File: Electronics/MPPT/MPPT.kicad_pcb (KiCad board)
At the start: 2 copper layers, 125 parts, among them J1 Solar Array, J2 Battery, J3 Car Power, J4 CAN_In, J5 CAN_Out, Q1 200N25N, Q2 200N25N, SW1 RESET, SW2 CAN Address, U1 PQMC3-D12-S9-S, U2 Nucleo_L432KC, U3 UCC37321, U4 INA213, U5 ADM3055E, U6 INA213, U7 CDSOT23-T24CAN

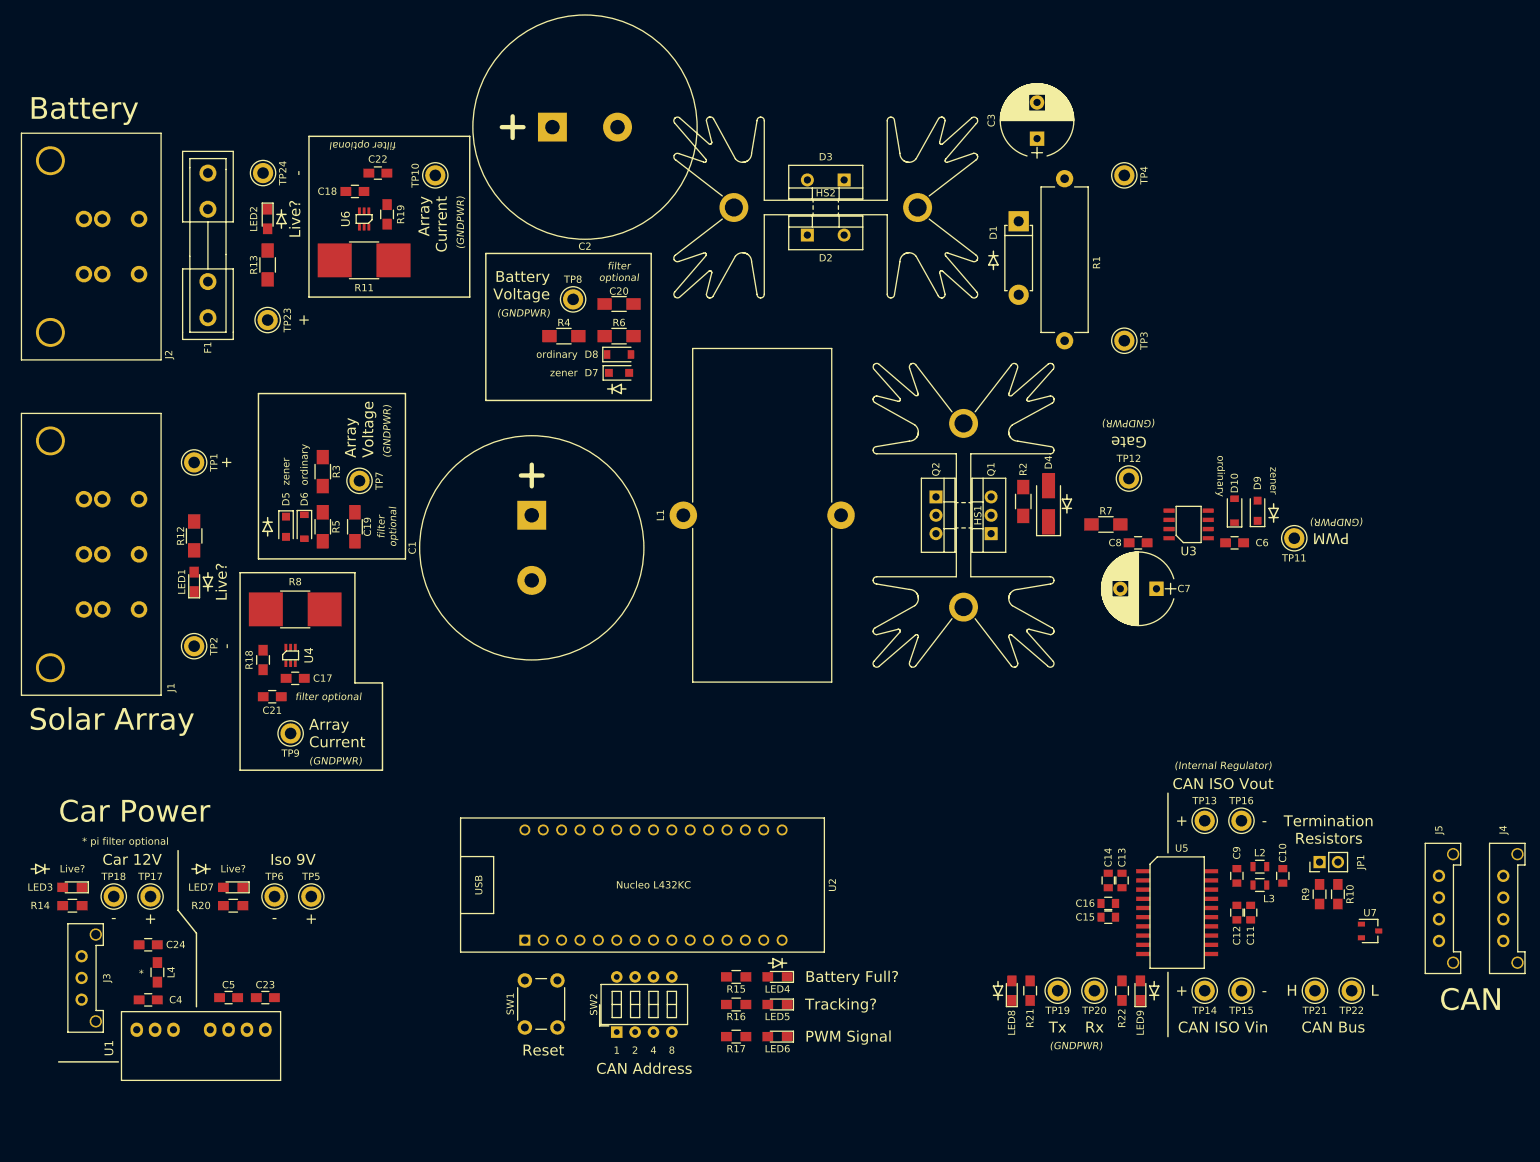
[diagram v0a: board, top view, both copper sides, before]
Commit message: MPPT: Laid out and wired much of the board. Could use much work still.
Still need to wire up CAN block and sensors; kicad is being funny about clearances around the INA chips. Also need to move filters closer to the Nucleo rather than centered around the sensors. Whole board could be compacted further.
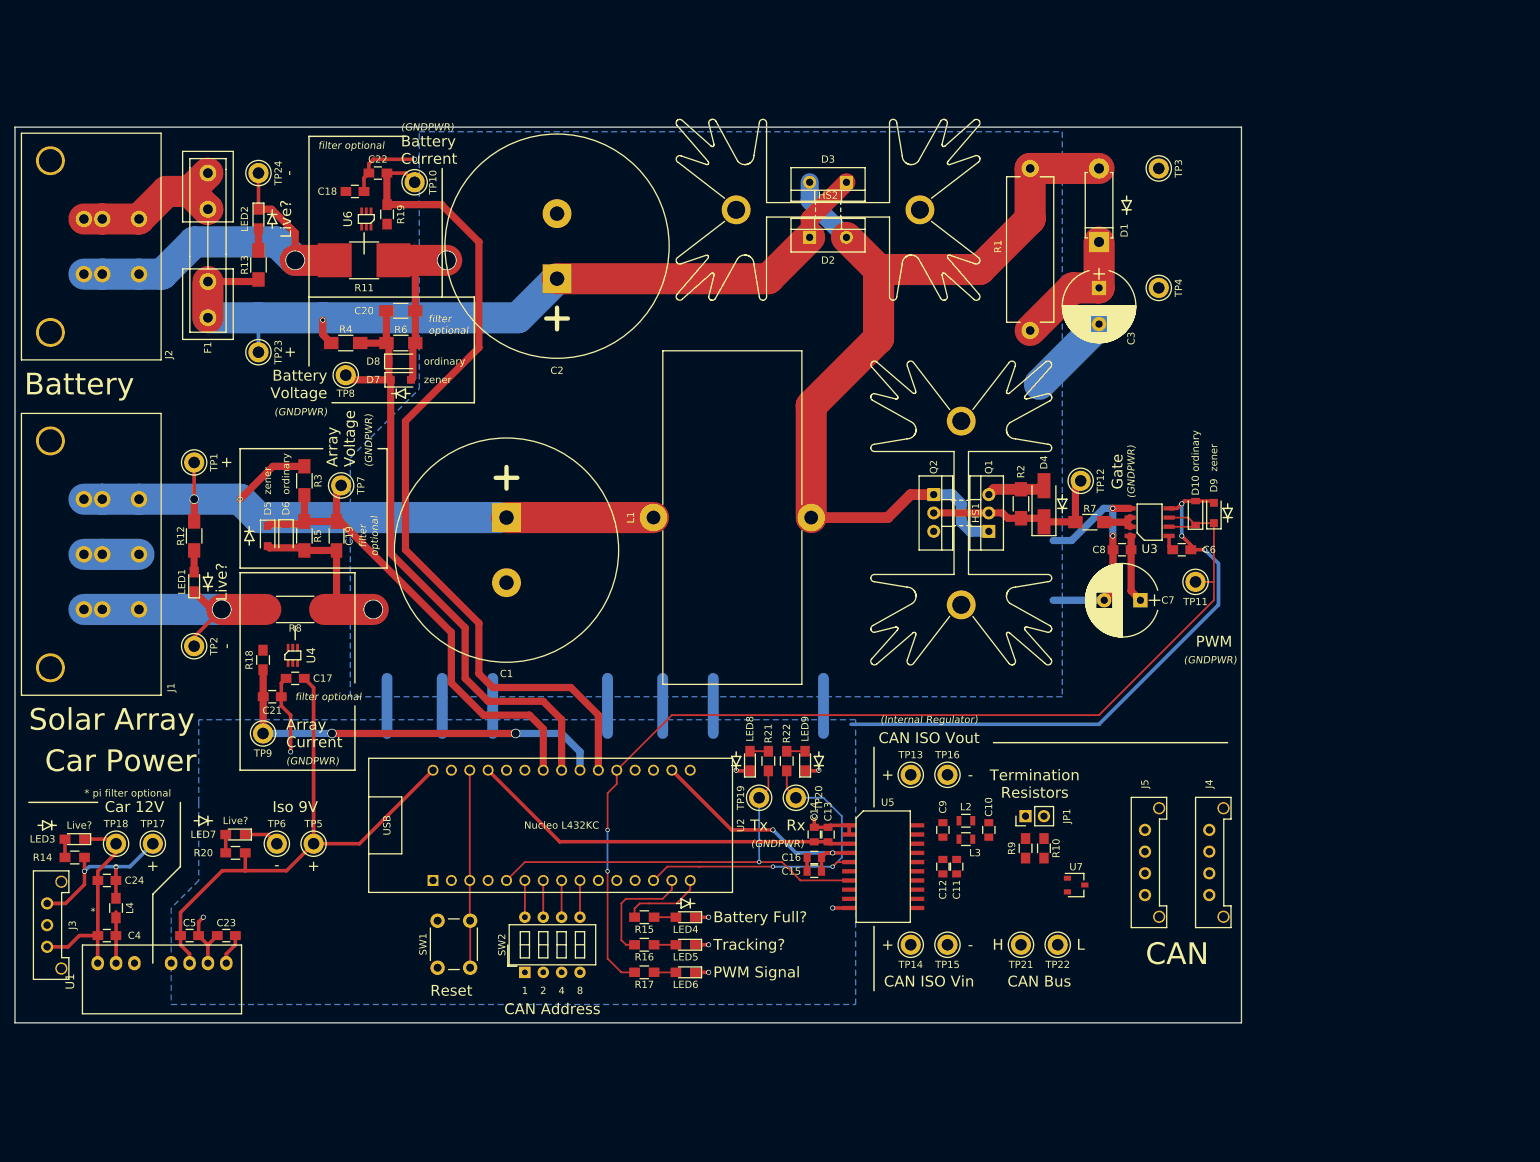
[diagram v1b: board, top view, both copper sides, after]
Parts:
- R8: footprint Resistors_SMD:R_2816_HandSoldering -> Resistors_SMD:R_2512_HandSoldering
- moved R22 56.2 mm to (137.8, 118.7)
- moved LED9 56.2 mm to (140.3, 118.7)
- moved REF** 56.2 mm to (142.2, 118.7)
- moved TP20 49.1 mm to (139.1, 123.8)
- moved TP19 49.1 mm to (134.0, 123.8)
- moved LED8 48.1 mm to (132.7, 118.7)
- moved R21 48.1 mm to (135.3, 118.7)
- moved REF** 48.1 mm to (130.8, 118.7)
- moved C11 41.1 mm to (161.3, 133.3)
- moved C12 41.1 mm to (159.4, 133.3)
- moved C13 41.1 mm to (143.5, 128.9)
- moved C14 41.1 mm to (141.6, 128.9)
- moved C15 41.1 mm to (141.6, 134.0)
- moved C16 41.1 mm to (141.6, 132.1)
- moved C9 41.1 mm to (159.4, 128.3)
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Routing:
- net GNDPWR: track 0.00 -> 240.6 mm, vias 0 -> 17
- net /PWM: track 0.00 -> 147.0 mm, vias 0 -> 2
- net Net-(D1-Pad2): track 0.00 -> 124.0 mm
- net /+Batt: track 0.00 -> 118.7 mm, vias 0 -> 1
- net /Battery_Current: track 0.00 -> 118.2 mm
- net /+Arr: track 0.00 -> 98.1 mm, vias 0 -> 2
- net /Battery_Voltage: track 0.00 -> 88.1 mm
- net +9VA: track 0.00 -> 88.0 mm
- net /Array_Voltage: track 0.00 -> 68.9 mm
- net /CAN_Tx: track 0.00 -> 62.6 mm, vias 0 -> 1
- net /Array_Current: track 0.00 -> 56.2 mm, vias 0 -> 2
- net +5V: track 0.00 -> 54.1 mm
- net (no net): track 0.00 -> 53.4 mm
- net /-Batt: track 0.00 -> 52.8 mm, vias 0 -> 1
- net /CAN_Rx: track 0.00 -> 47.3 mm, vias 0 -> 2
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- added copper zone on B.Cu, net GNDPWR
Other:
- board outline added: 169.5 x 123.8 mm
- net class HighPower added: clearance 0.5, trace_width 4.3, via_dia 2.7, via_drill 2.5
- net class HighPowerHalf added: clearance 0.3, trace_width 2.5, via_dia 2.7, via_drill 2.5
- net class HighPowerSignal added: clearance 0.2, trace_width 1, via_dia 1.3, via_drill 1.1
- net class HighPowerSmall added: clearance 0.2, trace_width 1.5, via_dia 1.8, via_drill 1.6
- net class LowPower added: clearance 0.2, trace_width 0.5, via_dia 0.7, via_drill 0.5
- net class Signal added: clearance 0.2, trace_width 0.25, via_dia 0.6, via_drill 0.4
- board text added: "Battery Current"

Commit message: MPPT: Import changes from schematic; move sensor filters to Nucleo; compact power electronics further.
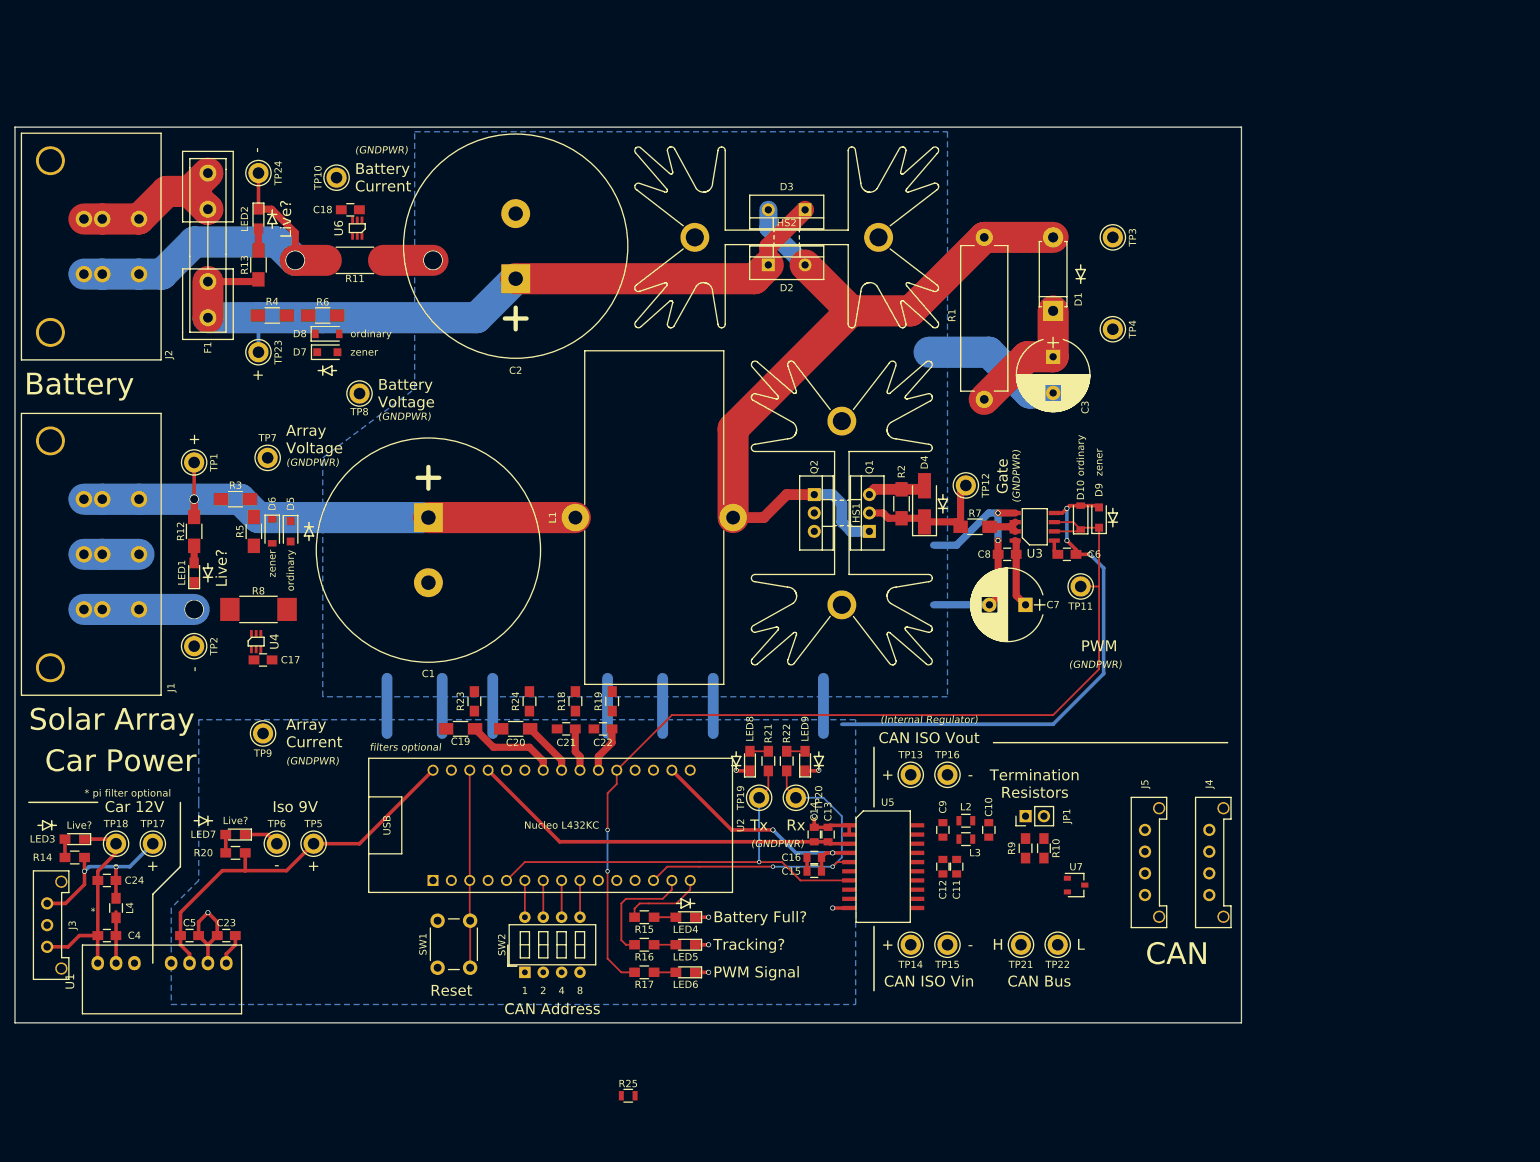
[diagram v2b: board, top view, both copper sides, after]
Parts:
- added R23: 1.7k, Resistors_SMD:R_0805_HandSoldering, F.Cu at (94.6, 110.5)
- added R24: 1.7k, Resistors_SMD:R_0805_HandSoldering, F.Cu at (102.2, 110.5)
- added R25: 0, Resistors_SMD:R_0805, F.Cu at (115.9, 165.0)
- C19, C20, C21, C22: value ?C -> 1uF
- R11: value 10m -> 2m; footprint Resistors_SMD:R_2816_HandSoldering -> Resistors_SMD:R_2512_HandSoldering
- R18, R19: value ?R -> 1.7k
- R8: value 10m -> 2m
- U4, U6: value INA213 -> INA210
- moved C22 82.9 mm to (112.4, 114.3)
- moved R19 74.2 mm to (113.7, 110.5), turned to 270 degrees
- moved C20 59.9 mm to (100.3, 114.3), turned to 180 degrees
- moved R18 43.6 mm to (108.6, 110.5)
- moved C21 40.9 mm to (107.3, 114.3), turned to 180 degrees
- moved C19 31.7 mm to (92.7, 114.3), turned to 180 degrees
- moved HS1 16.5 mm to (145.4, 84.5)
- moved Q1 16.5 mm to (149.2, 87.0)
- moved Q2 16.5 mm to (141.6, 81.9)
- moved R2 16.5 mm to (153.7, 83.2)
- moved REF** 16.5 mm to (159.4, 83.2)
- moved D4 16.5 mm to (156.8, 83.2)
- moved C6 15.9 mm to (176.5, 90.2)
- moved C7 15.9 mm to (170.8, 97.2)
- moved C8 15.9 mm to (168.3, 90.2)
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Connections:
- D5 pad 1: /Array_Voltage -> Net-(D5-Pad1)
- D6 pad 1: /Array_Voltage -> Net-(D5-Pad1)
- D7 pad 1: /Battery_Voltage -> Net-(D7-Pad1)
- D8 pad 1: /Battery_Voltage -> Net-(D7-Pad1)
- R3 pad 2: /Array_Voltage -> Net-(D5-Pad1)
- R4 pad 2: /Battery_Voltage -> Net-(D7-Pad1)
- R5 pad 1: /Array_Voltage -> Net-(D5-Pad1)
- R6 pad 1: /Battery_Voltage -> Net-(D7-Pad1)
- U5 pad 12: Net-(C10-Pad2) -> Net-(R25-Pad1)
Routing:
- net /Battery_Current: track 118.2 -> 6.50 mm
- net /Battery_Voltage: track 88.1 -> 7.52 mm
- net GNDPWR: track 240.6 -> 179.5 mm, vias 17 -> 14
- net /Array_Voltage: track 68.9 -> 12.5 mm
- net /Array_Current: track 56.2 -> 6.01 mm, vias 2 -> 0
- net +9VA: track 88.0 -> 64.6 mm
- net /+Arr: track 98.1 -> 75.9 mm, vias 2 -> 1
- net /-Arr: track 36.6 -> 16.5 mm
- net Net-(D1-Pad2): track 124.0 -> 109.9 mm
- net /+Batt: track 118.7 -> 107.7 mm, vias 1 -> 0
- net /PWM: track 147.0 -> 136.1 mm
- net /Drive_PWM: track 26.1 -> 19.5 mm
- net /-Batt: track 52.8 -> 51.6 mm
- net Net-(LED1-Pad2): track 3.00 -> 2.36 mm
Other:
- board text added: "filters optional"
- board text removed: "filter optional"

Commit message: MPPT: Shift Nucleo into more compact location; move sensor test points into position.
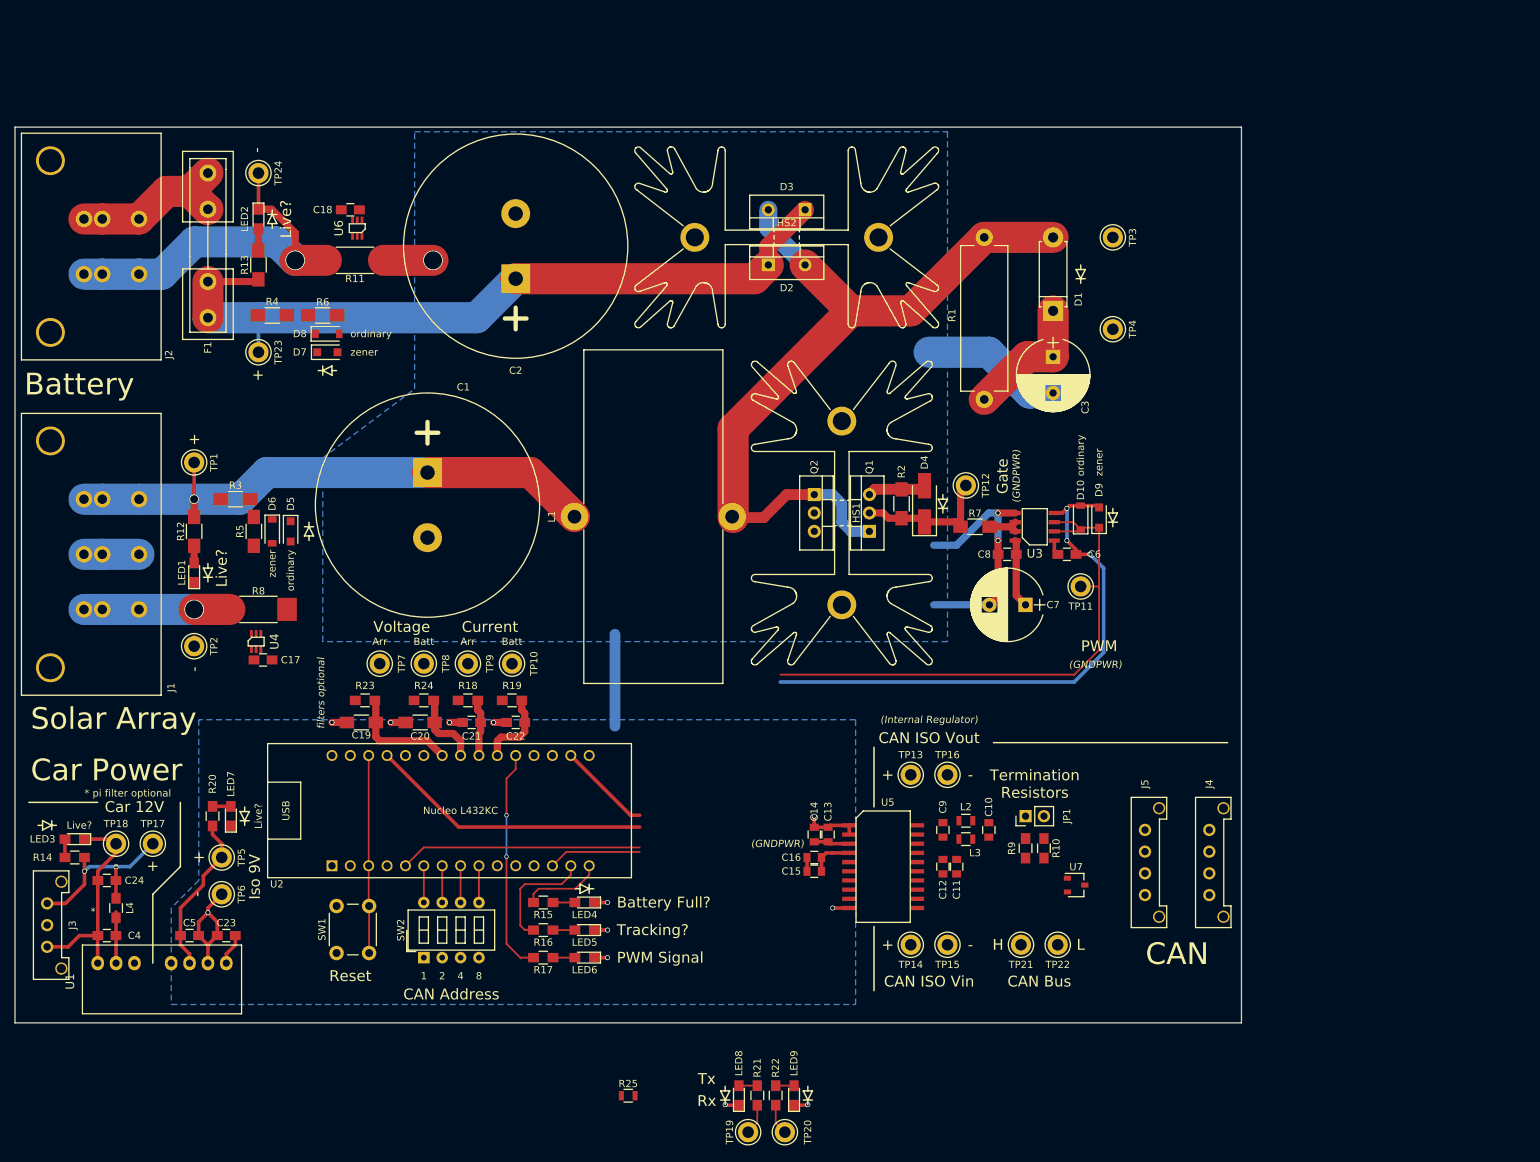
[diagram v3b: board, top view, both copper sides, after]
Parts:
- moved TP10 71.4 mm to (99.8, 105.3), turned to 180 degrees
- moved LED8 46.3 mm to (131.2, 165.0)
- moved LED9 46.3 mm to (138.8, 165.0)
- moved R21 46.3 mm to (133.7, 165.0)
- moved R22 46.3 mm to (136.3, 165.0)
- moved REF** 46.3 mm to (140.7, 165.0)
- moved REF** 46.3 mm to (129.3, 165.0)
- moved TP19 46.3 mm to (132.5, 170.1)
- moved TP20 46.3 mm to (137.5, 170.1)
- moved TP8 38.4 mm to (87.6, 105.3), turned to 180 degrees
- moved TP7 32.4 mm to (81.5, 105.3)
- moved TP9 29.9 mm to (93.7, 105.3), turned to 0 degrees
- moved R23 15.1 mm to (79.5, 110.4), turned to 0 degrees
- moved R18 14.9 mm to (93.7, 110.4), turned to 0 degrees
- moved R24 14.6 mm to (87.6, 110.4), turned to 0 degrees
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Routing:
- net (no net): track 53.4 -> 12.7 mm
- net +9VA: track 64.6 -> 34.0 mm
- net /CAN_Rx: track 47.3 -> 17.1 mm, vias 2 -> 0
- net /PWM: track 136.1 -> 106.5 mm
- net /CAN_Tx: track 62.6 -> 37.7 mm, vias 1 -> 0
- net +3V3: track 33.0 -> 18.9 mm, vias 2 -> 0
- net GNDPWR: track 179.5 -> 189.9 mm, vias 14 -> 18
- net +5V: track 54.1 -> 44.0 mm
- net /-Arr: track 16.5 -> 21.5 mm
- net /Battery_Current: track 6.50 -> 10.8 mm
- net /+Arr: track 75.9 -> 79.4 mm
- net /Battery_Voltage: track 7.52 -> 10.4 mm
- net /Array_Voltage: track 12.5 -> 15.3 mm
- net /Array_Current: track 6.01 -> 7.89 mm
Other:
- board text added: "Arr"
- board text added: "Batt"
- board text added: "Current"
- board text added: "Voltage"
- board text removed: "Array Current"
- board text removed: "Array Voltage"
- board text removed: "Battery Current"
- board text removed: "Battery Voltage"
